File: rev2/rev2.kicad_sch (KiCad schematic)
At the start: 4 parts, among them U1 STM32F030RCTx, Y1 16mhz

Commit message: added changes to the rev 2 board
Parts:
- removed U1: STM32F030RCTx, Package_QFP:LQFP-64_10x10mm_P0.5mm, symbol MCU_ST_STM32F0:STM32F030RCTx
- added U2: STM32H745ZGTx, Package_QFP:LQFP-144_20x20mm_P0.5mm, symbol MCU_ST_STM32H7:STM32H745ZGTx
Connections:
- net HSE_IN: now also U2.25 (PH0)
- net HSE_OUT: now also U2.26 (PH1)
- new net: U2.104 (VSS), U2.118 (VSS), U2.12 (VSS), U2.128 (VSS), U2.141 (VSS), U2.18 (VSS), U2.33 (VSS), U2.41 (VSS), U2.55 (VSS), U2.6 (VSS), U2.69 (VSS), U2.80 (VSS), U2.89 (VSS)
- new net +3.3V: U2.106 (VDD), U2.119 (VDD), U2.129 (VDD), U2.13 (VDD), U2.144 (VDD), U2.19 (VDD), U2.32 (VDD), U2.42 (VDD), U2.56 (VDD), U2.7 (VDD), U2.71 (VDD), U2.79 (VDD), U2.8 (VBAT), U2.92 (VDD)
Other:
- added sheet decouplingCapacitors (decoupling_sch.kicad_sch)

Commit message: something
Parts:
- removed C1, C2: C, symbol Device:C
- removed U2: STM32H745ZGTx, Package_QFP:LQFP-144_20x20mm_P0.5mm, symbol MCU_ST_STM32H7:STM32H745ZGTx
- removed Y1: 16mhz, symbol Device:Crystal_GND24
- added C22: 100n, Capacitor_SMD:C_0603_1608Metric_Pad1.08x0.95mm_HandSolder, symbol Device:C
- added C29, C30: 22u, Capacitor_SMD:C_0603_1608Metric_Pad1.08x0.95mm_HandSolder, symbol Device:C
- added D1: LED, LED_SMD:LED_0603_1608Metric_Pad1.05x0.95mm_HandSolder, symbol Device:LED
- added H1, H2, H3, H4: MountingHole, MountingHole:MountingHole_4.3mm_M4_Pad_Via, symbol Mechanical:MountingHole
- added R12: 2k2, Resistor_SMD:R_0603_1608Metric_Pad0.98x0.95mm_HandSolder, symbol Device:R_Small
- added SW1: Boot0, Button_Switch_SMD:SW_SPDT_CK-JS102011SAQN, symbol Switch:SW_SPDT
- added SW2: NRST, Button_Switch_SMD:SW_SPST_PTS645, symbol Switch:SW_Push
- added U1: STM32F429ZITx, Package_QFP:LQFP-144_20x20mm_P0.5mm, symbol MCU_ST_STM32F4:STM32F429ZITx
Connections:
- net +3.3V: now also SW1.1 (A), U1.108 (VDD), U1.121 (VDD), U1.131 (VDD), U1.143 (PDR_ON), U1.144 (VDD), U1.17 (VDD), U1.30 (VDD), U1.39 (VDD), U1.52 (VDD), U1.6 (VBAT), U1.62 (VDD), U1.72 (VDD), U1.84 (VDD), U1.95 (VDD)
- net GND: now also C22.2, C29.2, C30.2, R12.1, SW1.3 (C), SW2.1, U1.107 (VSS), U1.120 (VSS), U1.130 (VSS), U1.16 (VSS), U1.31 (VSSA), U1.38 (VSS), U1.51 (VSS), U1.61 (VSS), U1.83 (VSS), U1.94 (VSS)
- net HSE_OUT: now also U1.24 (PH1)
- new net: C30.1, U1.71 (VCAP_1)
- new net: D1.2 (A), U1.1 (PE2)
- new net: C29.1, U1.106 (VCAP_2)
- new net: D1.1 (K), R12.2
- new net +3.3VA: U1.32 (VREF+), U1.33 (VDDA)
- new net ADC1_IN14: U1.44 (PC4)
- new net ADC1_IN15: U1.45 (PC5)
- new net ADC1_IN8: U1.46 (PB0)
- new net ADC1_IN9: U1.47 (PB1)
- new net ADC2_IN4: U1.40 (PA4)
- new net ADC2_IN5: U1.41 (PA5)
- new net ADC2_IN6: U1.42 (PA6)
- new net ADC2_IN7: U1.43 (PA7)
- new net BOOT0: SW1.2 (B), U1.138 (BOOT0)
- new net CAN SIlent Mode 1: U1.116 (PD2)
- new net CAN SIlent Mode 2: U1.76 (PB15)
- new net CAN1_RX: U1.114 (PD0)
- new net CAN1_TX: U1.115 (PD1)
- new net CAN2_RX: U1.73 (PB12)
- new net CAN2_TX: U1.74 (PB13)
- new net HSE_IN  : U1.23 (PH0)
- new net I2C1_SCL: U1.139 (PB8)
- new net I2C1_SDA: U1.140 (PB9)
- new net I2C2_SCL: U1.11 (PF1)
- new net I2C2_SDA: U1.10 (PF0)
- new net MCU_GPIO1: U1.93 (PG8)
- new net MCU_GPIO10: U1.82 (PD13)
- new net MCU_GPIO2: U1.92 (PG7)
- new net MCU_GPIO3: U1.91 (PG6)
- new net MCU_GPIO4: U1.90 (PG5)
- new net MCU_GPIO5: U1.89 (PG4)
- new net MCU_GPIO6: U1.88 (PG3)
- new net MCU_GPIO7: U1.87 (PG2)
- new net MCU_GPIO8: U1.86 (PD15)
- new net MCU_GPIO9: U1.85 (PD14)
- new net NRST: C22.1, SW2.2, U1.25 (NRST)
- new net SPI3_CS  : U1.124 (PG9)
- new net SPI3_MISO: U1.112 (PC11)
- new net SPI3_MOSI: U1.113 (PC12)
- new net SPI3_SCK: U1.111 (PC10)
- new net SPI5_CS  : U1.18 (PF6)
- new net SPI5_MISO: U1.20 (PF8)
- new net SPI5_MOSI: U1.21 (PF9)
- new net SPI5_SCK : U1.19 (PF7)
- new net SYS_JTCLK-SWCLK: U1.109 (PA14)
- new net SYS_JTDO-SWO: U1.133 (PB3)
- new net SYS_JTMS-SWDIO: U1.105 (PA13)
- new net USART1_RX: U1.137 (PB7)
- new net USART1_TX: U1.136 (PB6)
- new net USB_OTG_FS_DP+: U1.104 (PA12)
- new net USB_OTG_FS_DP-: U1.103 (PA11)
- new net logging: U1.36 (PA2)
- no-connect marks 0 -> 67
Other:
- removed sheet decouplingCapacitors
- added sheet CAN (CAN.kicad_sch)
- added sheet HSE (HSE.kicad_sch)
- added sheet USB (USB.kicad_sch)
- added sheet connectors (connectors.kicad_sch)
- added sheet power (power_sch.kicad_sch)
- note added: "Low ESR Caps"
- note added: "Toggle LED"

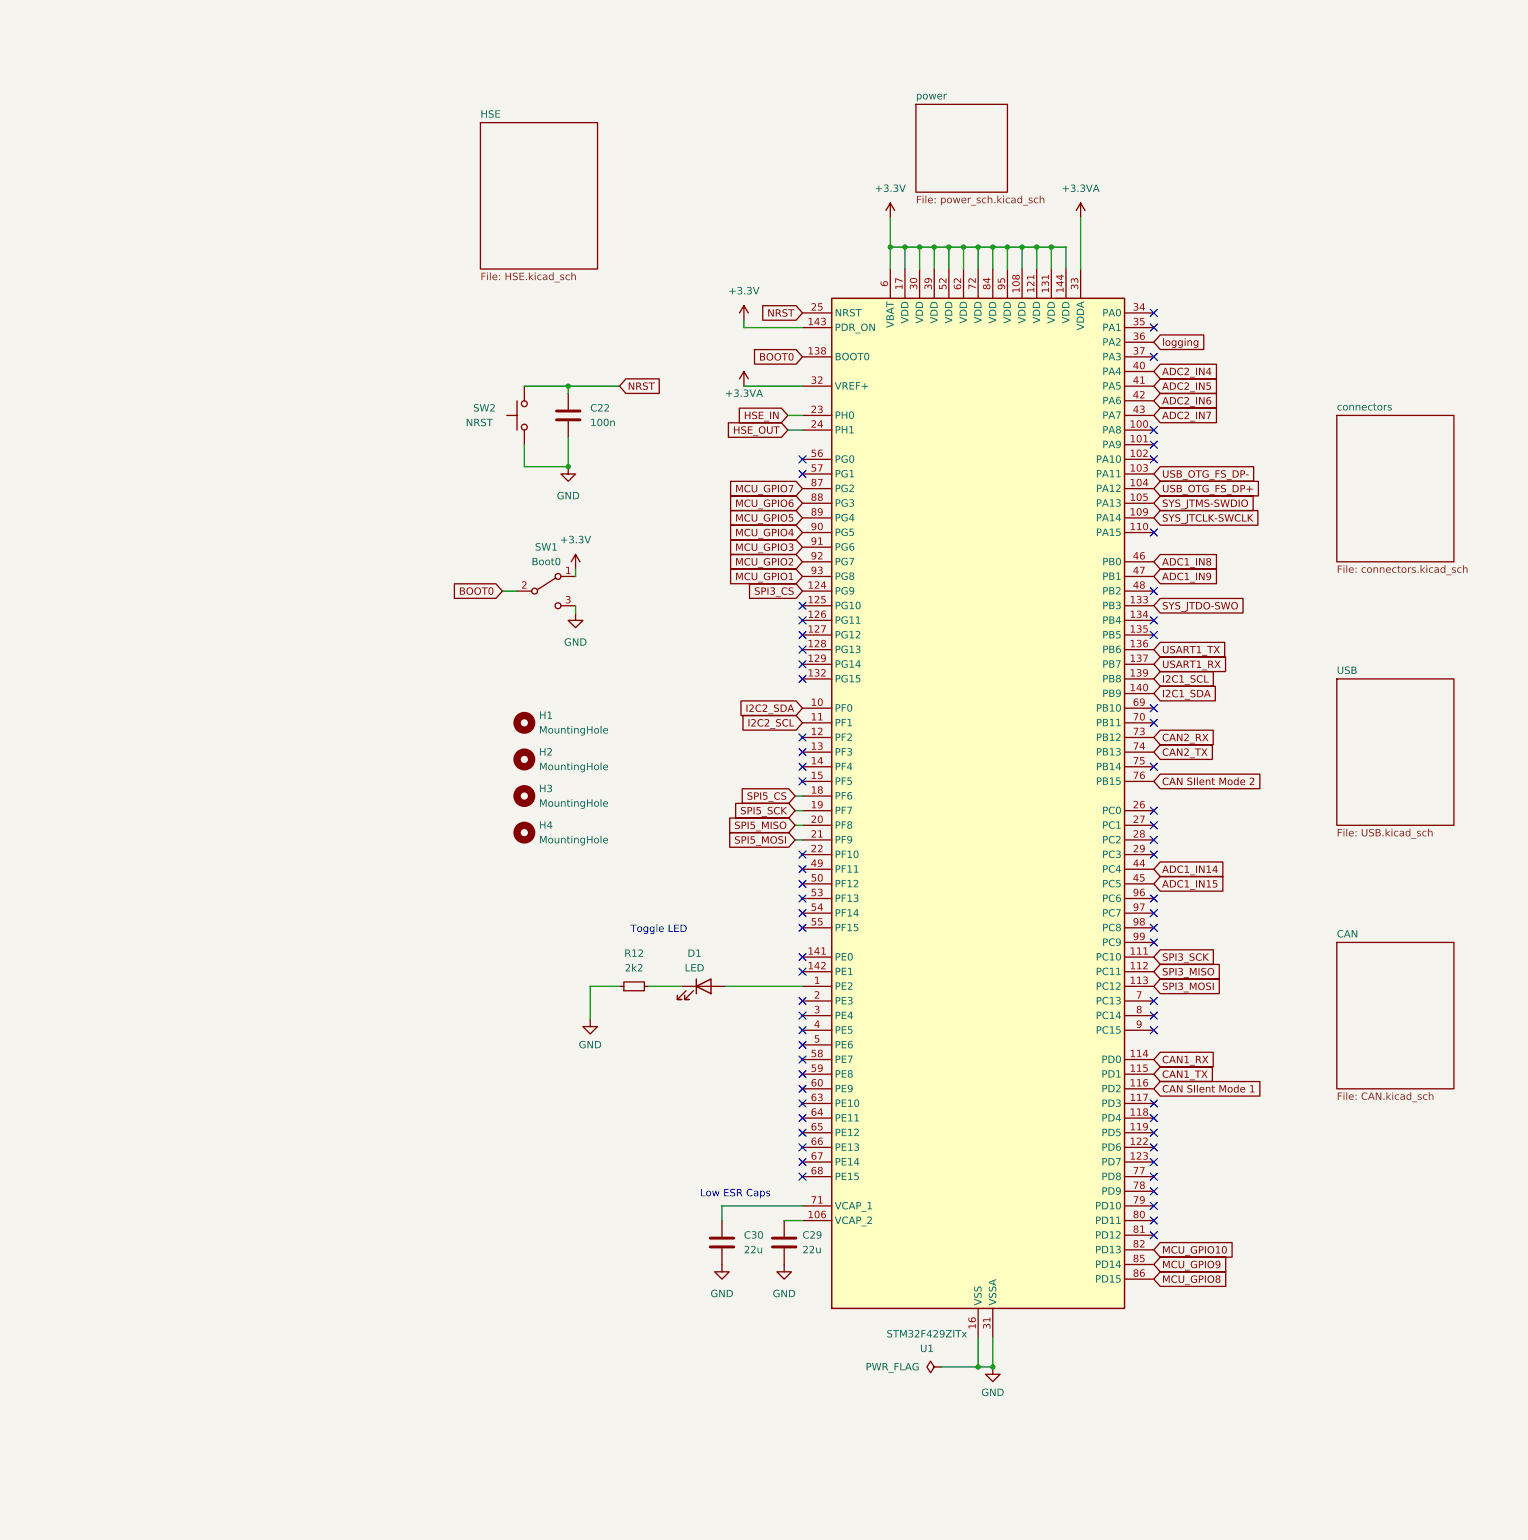
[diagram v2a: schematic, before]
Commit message: started the rev 2 design with basic stm32 necessary circuits
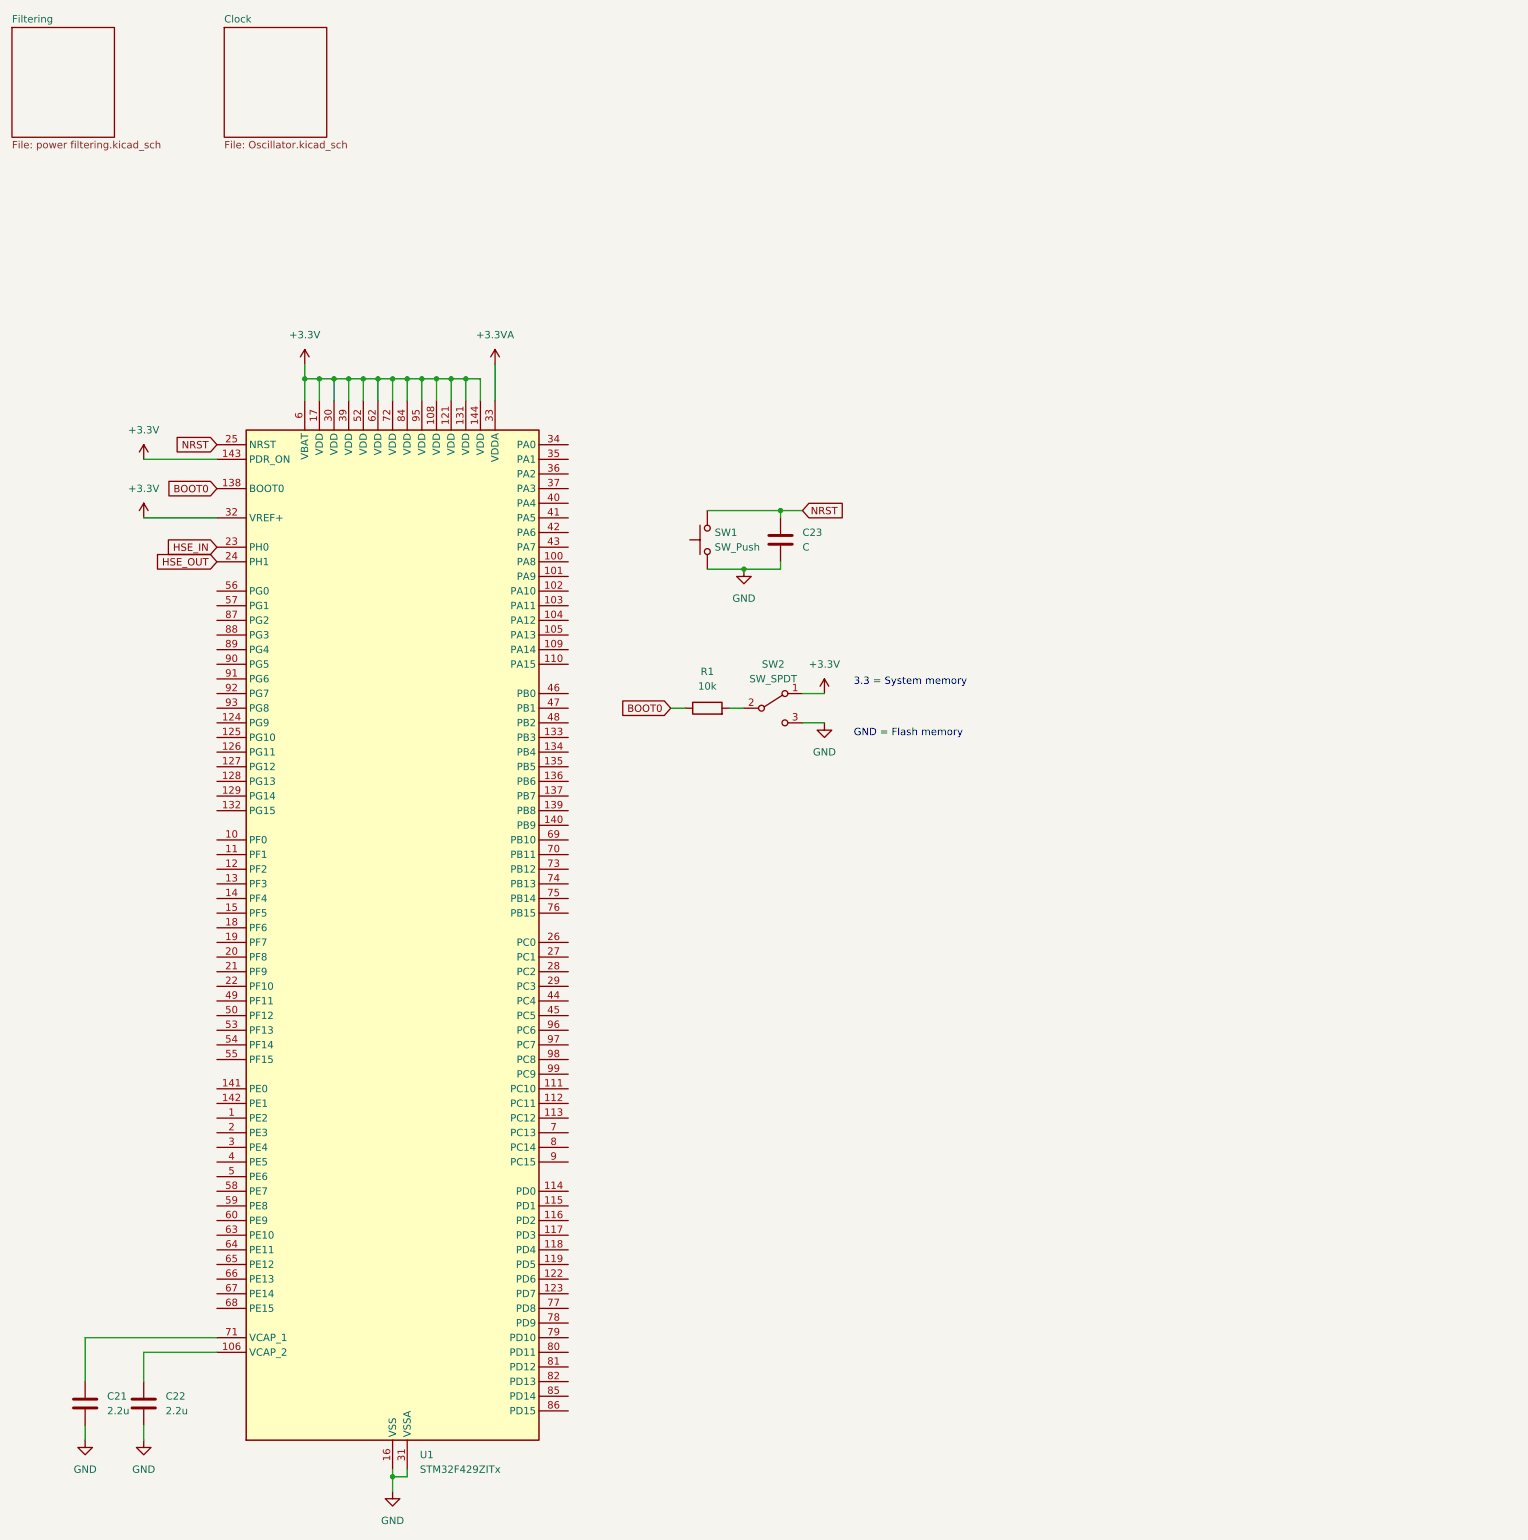
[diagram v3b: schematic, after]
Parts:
- removed C29, C30: 22u, Capacitor_SMD:C_0603_1608Metric_Pad1.08x0.95mm_HandSolder, symbol Device:C
- removed D1: LED, LED_SMD:LED_0603_1608Metric_Pad1.05x0.95mm_HandSolder, symbol Device:LED
- removed H1, H2, H3, H4: MountingHole, MountingHole:MountingHole_4.3mm_M4_Pad_Via, symbol Mechanical:MountingHole
- removed R12: 2k2, Resistor_SMD:R_0603_1608Metric_Pad0.98x0.95mm_HandSolder, symbol Device:R_Small
- removed SW1: Boot0, Button_Switch_SMD:SW_SPDT_CK-JS102011SAQN, symbol Switch:SW_SPDT
- removed SW2: NRST, Button_Switch_SMD:SW_SPST_PTS645, symbol Switch:SW_Push
- added C21: 2.2u, symbol Device:C
- added C23: C, symbol Device:C
- added R1: 10k, symbol Device:R
- added SW1: SW_Push, symbol Switch:SW_Push
- added SW2: SW_SPDT, symbol Switch:SW_SPDT
- C22: value 100n -> 2.2u; footprint Capacitor_SMD:C_0603_1608Metric_Pad1.08x0.95mm_HandSolder -> (none); JLCpart# C76599 -> (none)
- U1: JLCpart# C92002 -> (none)
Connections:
- net +3.3V: now also U1.32 (VREF+), SW2.1 (A)
- net +3.3VA: no longer U1.32 (VREF+)
- net BOOT0: now also R1.1
- net GND: now also C21.2, C23.2, SW1.1, SW2.3 (C)
- net NRST: now also C23.1, SW1.2; no longer C22.1
- net at U1.71 (VCAP_1): now also C21.1
- net at U1.106 (VCAP_2): now also C22.1
- net ADC1_IN14: no longer names the net of U1.44 (PC4)
- net ADC1_IN15: no longer names the net of U1.45 (PC5)
- net ADC1_IN8: no longer names the net of U1.46 (PB0)
- net ADC1_IN9: no longer names the net of U1.47 (PB1)
- net ADC2_IN4: no longer names the net of U1.40 (PA4)
- net ADC2_IN5: no longer names the net of U1.41 (PA5)
- net ADC2_IN6: no longer names the net of U1.42 (PA6)
- net ADC2_IN7: no longer names the net of U1.43 (PA7)
- net CAN SIlent Mode 1: no longer names the net of U1.116 (PD2)
- net CAN SIlent Mode 2: no longer names the net of U1.76 (PB15)
- net CAN1_RX: no longer names the net of U1.114 (PD0)
- net CAN1_TX: no longer names the net of U1.115 (PD1)
- net CAN2_RX: no longer names the net of U1.73 (PB12)
- net CAN2_TX: no longer names the net of U1.74 (PB13)
- net HSE_IN   renamed HSE_IN
- net I2C1_SCL: no longer names the net of U1.139 (PB8)
- net I2C1_SDA: no longer names the net of U1.140 (PB9)
- net I2C2_SCL: no longer names the net of U1.11 (PF1)
- net I2C2_SDA: no longer names the net of U1.10 (PF0)
- net MCU_GPIO1: no longer names the net of U1.93 (PG8)
- net MCU_GPIO10: no longer names the net of U1.82 (PD13)
- net MCU_GPIO2: no longer names the net of U1.92 (PG7)
- net MCU_GPIO3: no longer names the net of U1.91 (PG6)
- net MCU_GPIO4: no longer names the net of U1.90 (PG5)
- net MCU_GPIO5: no longer names the net of U1.89 (PG4)
- net MCU_GPIO6: no longer names the net of U1.88 (PG3)
- net MCU_GPIO7: no longer names the net of U1.87 (PG2)
- net MCU_GPIO8: no longer names the net of U1.86 (PD15)
- net MCU_GPIO9: no longer names the net of U1.85 (PD14)
- net SPI3_CS  : no longer names the net of U1.124 (PG9)
- net SPI3_MISO: no longer names the net of U1.112 (PC11)
- net SPI3_MOSI: no longer names the net of U1.113 (PC12)
- net SPI3_SCK: no longer names the net of U1.111 (PC10)
- net SPI5_CS  : no longer names the net of U1.18 (PF6)
- net SPI5_MISO: no longer names the net of U1.20 (PF8)
- net SPI5_MOSI: no longer names the net of U1.21 (PF9)
- net SPI5_SCK : no longer names the net of U1.19 (PF7)
- net SYS_JTCLK-SWCLK: no longer names the net of U1.109 (PA14)
- net SYS_JTDO-SWO: no longer names the net of U1.133 (PB3)
- net SYS_JTMS-SWDIO: no longer names the net of U1.105 (PA13)
- net USART1_RX: no longer names the net of U1.137 (PB7)
- net USART1_TX: no longer names the net of U1.136 (PB6)
- net USB_OTG_FS_DP+: no longer names the net of U1.104 (PA12)
- net USB_OTG_FS_DP-: no longer names the net of U1.103 (PA11)
- net logging: no longer names the net of U1.36 (PA2)
- new net: R1.2, SW2.2 (B)
- no-connect marks 67 -> 0
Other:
- removed sheet CAN
- removed sheet HSE
- removed sheet USB
- removed sheet connectors
- removed sheet power
- added sheet Clock (Oscillator.kicad_sch)
- added sheet Filtering (power filtering.kicad_sch)
- note added: "3.3 = System memory"
- note added: "GND = Flash memory"
- note removed: "Low ESR Caps"
- note removed: "Toggle LED"

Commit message: done most of the schematic. I think I just need to do USB, Maybe SPI ( if needed),USB data, and some more I2C lines or another UART
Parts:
- added C24, C25: 9p, Capacitor_SMD:C_0603_1608Metric, symbol Device:C_Small
- added C24: 100n, symbol Device:C_Small
- added C25: 500n, symbol Device:C
- added C28: 10u, symbol Device:C
- added C29: 22u, symbol Device:C
- added J1, J3: Termination, symbol Connector:Conn_01x02_Pin
- added J2: CAN1, symbol Connector:Screw_Terminal_01x02
- added J4: CAN2, symbol Connector:Screw_Terminal_01x02
- added J5: SWD ASYNC, symbol Connector_Generic:Conn_02x05_Odd_Even
- added J6: LIN Pots, symbol Connector:Screw_Terminal_01x04
- added J7: AIN, symbol Connector:Screw_Terminal_01x04
- added R2: 47, Resistor_SMD:R_0603_1608Metric, symbol Device:R_Small
- added R2, R6, R7, R8: 100, symbol Device:R_Small
- added R4, R5: 120, symbol Device:R_Small
- added U2, U3: TJA1051T, Package_SO:SOIC-8_3.9x4.9mm_P1.27mm, symbol Interface_CAN_LIN:TJA1051T
- added U4: ~, symbol custom parts library:LSM6DSOX
- added U5: AMS1117-3.3, Package_TO_SOT_SMD:SOT-223-3_TabPin2, symbol Regulator_Linear:AMS1117-3.3
- added Y3: 16MHz, Crystal:Crystal_SMD_3225-4Pin_3.2x2.5mm, symbol Device:Crystal_GND24
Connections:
- net +3.3VA is gone; now on net +3.3V: U1.33 (VDDA)
- net +3.3V: now also C24.2, C25.1, C29.1, J5.1 (Pin_1), U4.8 (VDD), U5.2 (VO)
- net GND: now also C24.1, C24.2, C25.2, C25.2, C28.2, C29.2, J5.3 (Pin_3), J5.5 (Pin_5), J5.9 (Pin_9), U2.2 (GND), U3.2 (GND), U4.2 (SDX), U4.3 (SCX), U4.6 (GND), U4.7 (GND), U5.1 (GND), Y3.2, Y3.4
- net HSE_IN: now also C24.1, Y3.1
- net HSE_OUT: now also R2.1
- net NRST: now also R8.2
- net CAN1_RX: now reaches U1.103 (PA11)
- net CAN1_RX: now also U2.4 (RXD)
- net CAN1_TX: now reaches U1.104 (PA12)
- net CAN1_TX: now also U2.1 (TXD)
- net SYS_JTMS_SWDIO: now reaches U1.105 (PA13)
- net SYS_JTMS_SWDIO: now also R2.2
- net SYS_JTCK_SWCLK: now reaches U1.109 (PA14)
- net SYS_JTCK_SWCLK: now also R6.2
- net Silent Mode 1: now reaches U1.110 (PA15)
- net Silent Mode 1: now also U2.8 (S)
- net GPIO7: now reaches U1.123 (PD7)
- net GPIO6: now reaches U1.124 (PG9)
- net GPIO5: now reaches U1.125 (PG10)
- net GPIO4: now reaches U1.126 (PG11)
- net GPIO3: now reaches U1.127 (PG12)
- net GPIO2: now reaches U1.128 (PG13)
- net GPIO1: now reaches U1.129 (PG14)
- net SYS_JTDO_SWO: now reaches U1.133 (PB3)
- net SYS_JTDO_SWO: now also R7.2
- net INT1: now reaches U1.135 (PB5)
- net INT1: now also U4.4 (INT1)
- net LSM_SCL: now reaches U1.136 (PB6)
- net LSM_SCL: now also U4.13 (SCL)
- net LSM_SDA: now reaches U1.137 (PB7)
- net LSM_SDA: now also U4.14 (SDA)
- net LSM_SDO: now reaches U1.139 (PB8)
- net LSM_SDO: now also U4.1 (SD0)
- net LSM_CS: now reaches U1.140 (PB9)
- net LSM_CS: now also U4.12 (CS)
- net at U1.34 (PA0): now also J6.1 (Pin_1)
- net at U1.35 (PA1): now also J6.2 (Pin_2)
- net at U1.36 (PA2): now also J6.3 (Pin_3)
- net at U1.37 (PA3): now also J6.4 (Pin_4)
- net at U1.40 (PA4): now also J7.1 (Pin_1)
- net at U1.41 (PA5): now also J7.2 (Pin_2)
- net at U1.42 (PA6): now also J7.3 (Pin_3)
- net at U1.43 (PA7): now also J7.4 (Pin_4)
- net CAN2_RX: now reaches U1.73 (PB12)
- net CAN2_RX: now also U3.4 (RXD)
- net CAN2_TX: now reaches U1.74 (PB13)
- net CAN2_TX: now also U3.1 (TXD)
- net Silent Mode 2: now reaches U1.75 (PB14)
- net Silent Mode 2: now also U3.8 (S)
- net GPIO8: now reaches U1.77 (PD8)
- new net: C25.1, R2.2, Y3.3
- new net: J5.6 (Pin_6), R7.1
- new net: J5.10 (Pin_10), R8.1
- new net: J5.2 (Pin_2), R2.1
- new net: J5.4 (Pin_4), R6.1
- new net +5V: C28.1, U2.3 (VCC), U3.3 (VCC), U5.3 (VI)
- new net CANH1+: J1.2 (Pin_2), J2.1 (Pin_1), R4.2, U2.7 (CANH)
- new net CANH2+: J3.2 (Pin_2), J4.1 (Pin_1), R5.2, U3.7 (CANH)
- new net CANL1-: J1.1 (Pin_1), J2.2 (Pin_2), R4.1, U2.6 (CANL)
- new net CANL2-: J3.1 (Pin_1), J4.2 (Pin_2), R5.1, U3.6 (CANL)
- no-connect marks 0 -> 87
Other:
- removed sheet Clock
- note added: "GPIO to Toggle Silent Mode"
- note added: "Power"
- note added: "SWD"
- note added: "uC clock"
- title: (none) -> DAQ
- moved on the sheet: C21, C22, C23, R1, SW1, SW2, U1
